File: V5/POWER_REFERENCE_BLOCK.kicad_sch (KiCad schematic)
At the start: 32 parts, among them J201 3xAA_BATTERY, Q201 PMV48XP, SW201 MAIN_PWR_SW, U201 MCP3208-CI/P, U202 MCP6002-xP, U203 TPS7A2033PDBVR, U204 TPS22917DBVR

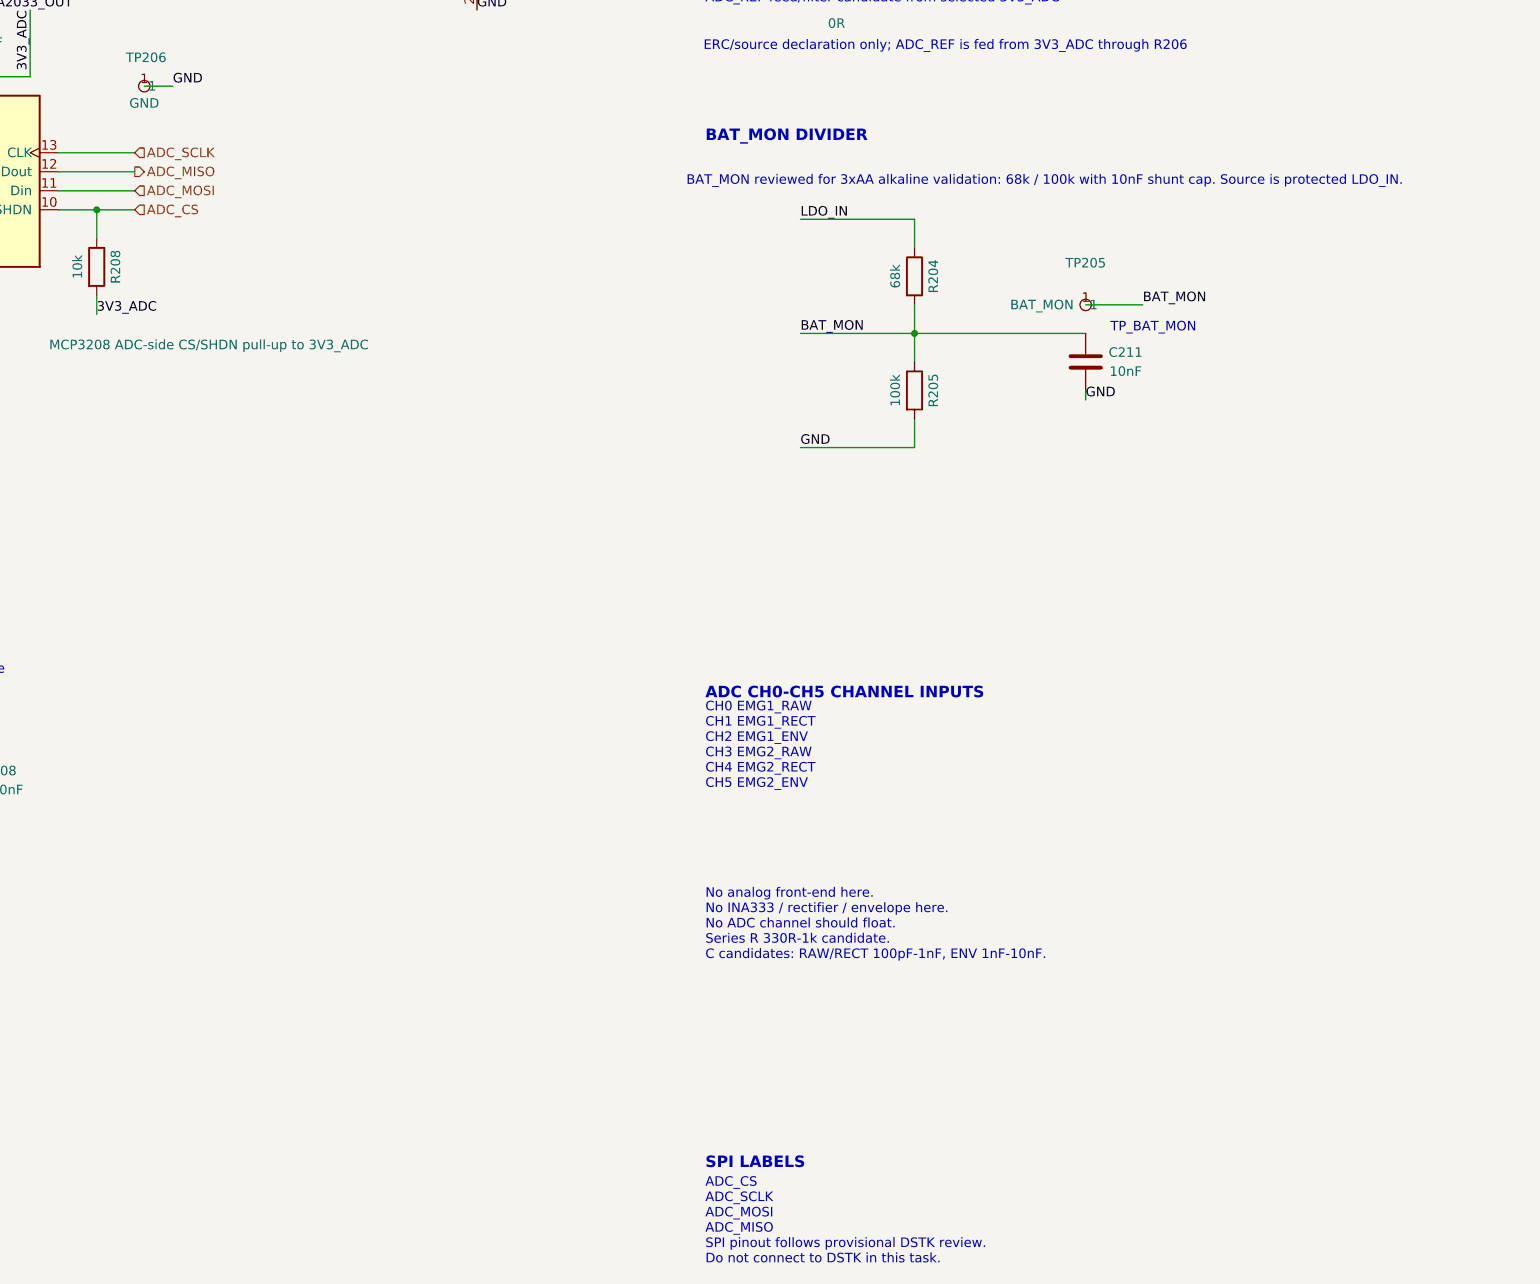
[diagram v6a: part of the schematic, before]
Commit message: add unequal-power spi isolation
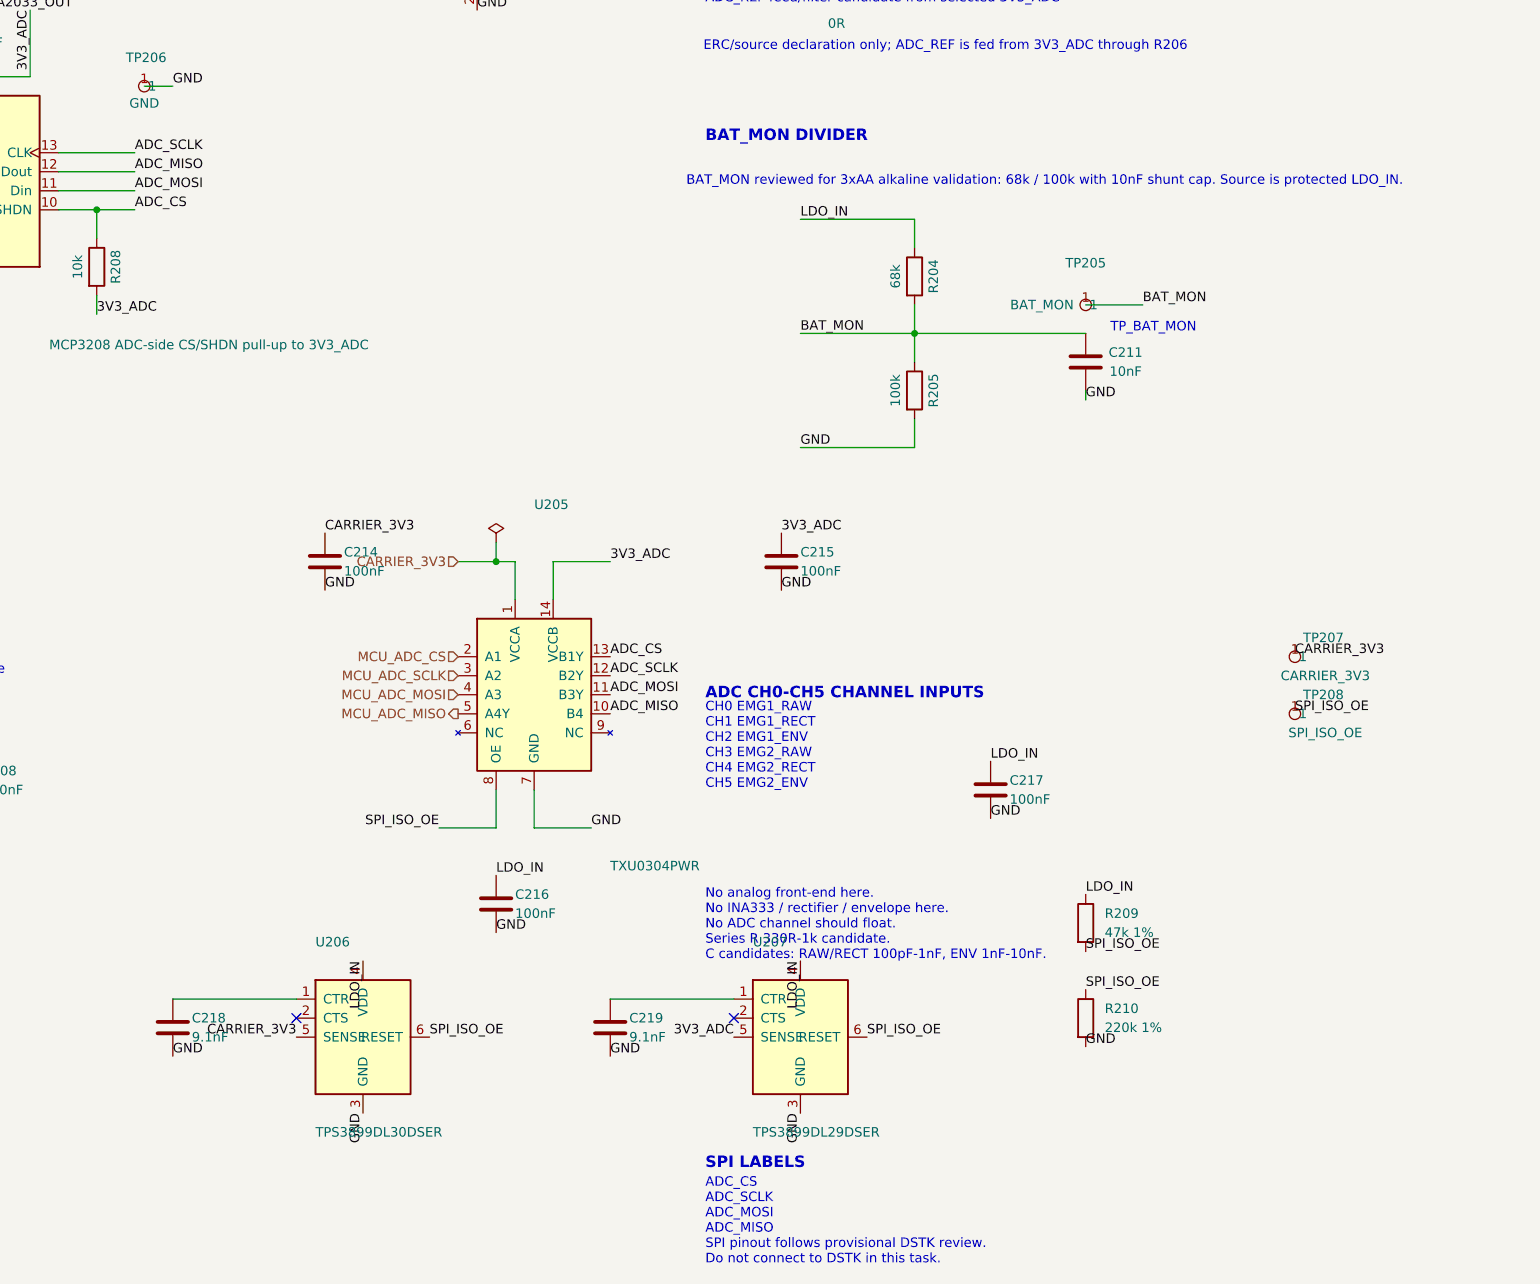
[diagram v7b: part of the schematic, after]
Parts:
- added C214, C215, C216, C217: 100nF, Capacitor_SMD:C_0603_1608Metric, symbol Device:C
- added C218, C219: 9.1nF, Capacitor_SMD:C_0603_1608Metric, symbol Device:C
- added R209: 47k 1%, Resistor_SMD:R_0603_1608Metric, symbol Device:R
- added R210: 220k 1%, Resistor_SMD:R_0603_1608Metric, symbol Device:R
- added TP207: CARRIER_3V3, TestPoint:TestPoint_Pad_D1.0mm, symbol EMG_V5:EMG_TestPoint
- added TP208: SPI_ISO_OE, TestPoint:TestPoint_Pad_D1.0mm, symbol EMG_V5:EMG_TestPoint
- added U205: TXU0304PWR, Package_SO:TSSOP-14_4.4x5mm_P0.65mm, symbol EMG_V5:TXU0304PWR
- added U206: TPS3899DL30DSER, Package_SON:WSON-6_1.5x1.5mm_P0.5mm, symbol EMG_V5:TPS3899DL_DSE
- added U207: TPS3899DL29DSER, Package_SON:WSON-6_1.5x1.5mm_P0.5mm, symbol EMG_V5:TPS3899DL_DSE
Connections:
- net 3V3_ADC: now also C215.1, U205.14 (VCCB), U207.5 (SENSE)
- net ADC_CS: now also U205.13 (B1Y)
- net ADC_MISO: now also U205.10 (B4)
- net ADC_MOSI: now also U205.11 (B3Y)
- net ADC_SCLK: now also U205.12 (B2Y)
- net GND: now also C214.2, C215.2, C216.2, C217.2, C218.2, C219.2, R210.2, U205.7 (GND), U206.3 (GND), U207.3 (GND)
- net LDO_IN: now also C216.1, C217.1, R209.1, U206.4 (VDD), U207.4 (VDD)
- new net: C218.1, U206.1 (CTR)
- new net: C219.1, U207.1 (CTR)
- new net CARRIER_3V3: C214.1, TP207.1, U205.1 (VCCA), U206.5 (SENSE)
- new net MCU_ADC_CS: U205.2 (A1)
- new net MCU_ADC_MISO: U205.5 (A4Y)
- new net MCU_ADC_MOSI: U205.4 (A3)
- new net MCU_ADC_SCLK: U205.3 (A2)
- new net SPI_ISO_OE: R209.2, R210.1, TP208.1, U205.8 (OE), U206.6 (RESET), U207.6 (RESET)
- no-connect marks 2 -> 4
